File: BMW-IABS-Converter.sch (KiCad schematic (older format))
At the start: 43 parts, among them J1 SWD, J2 BMW_MOTORRAD, Q1 IRLML0060TRPbF, Q2 IRLML0060TRPbF, Q4 IRFR9024, Q6 IRFR9024, U1 SN65HVD230, U2 STM32F042F4P6, U3 MC34063AD, U4 LM2904

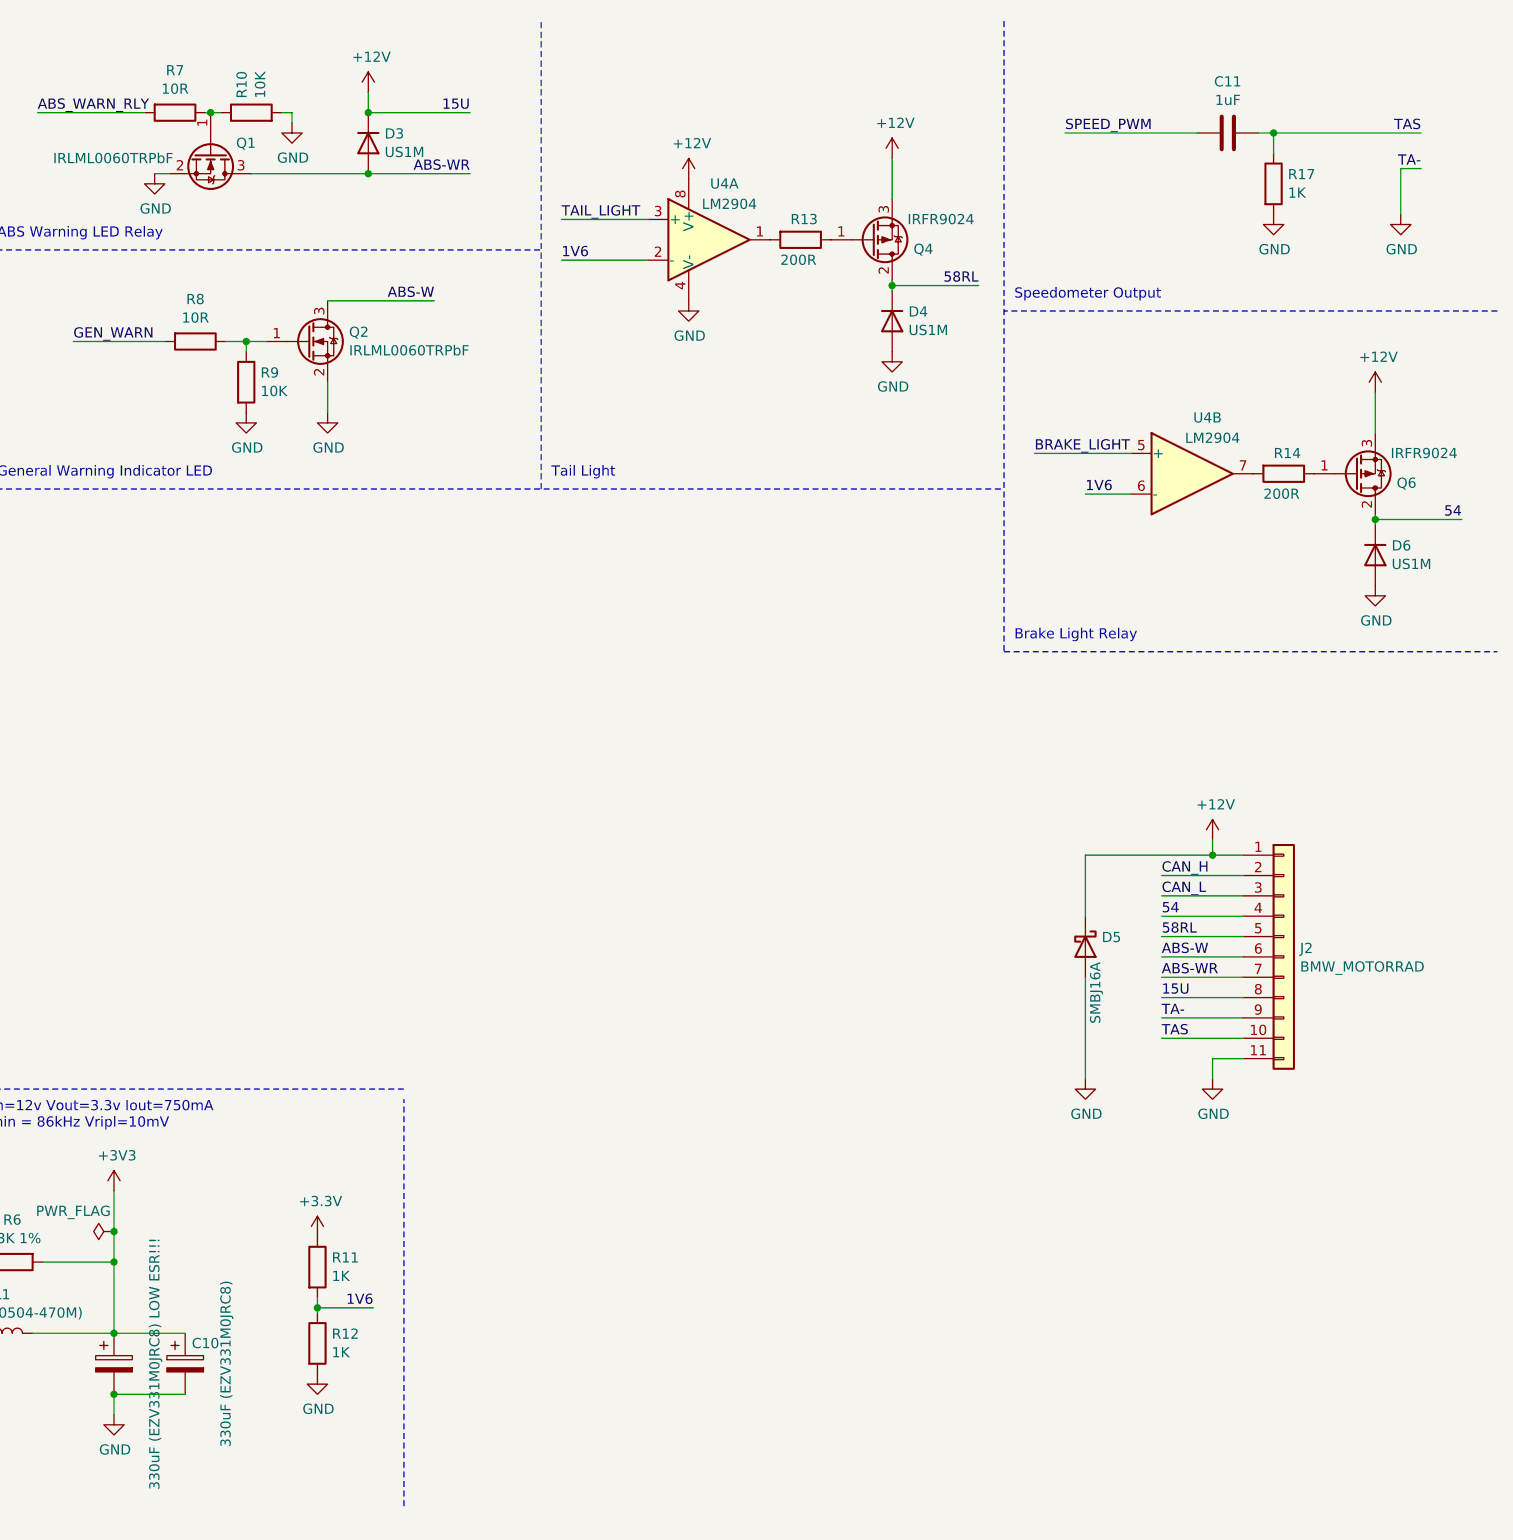
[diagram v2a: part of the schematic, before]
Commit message: Added connector footprint and symbol
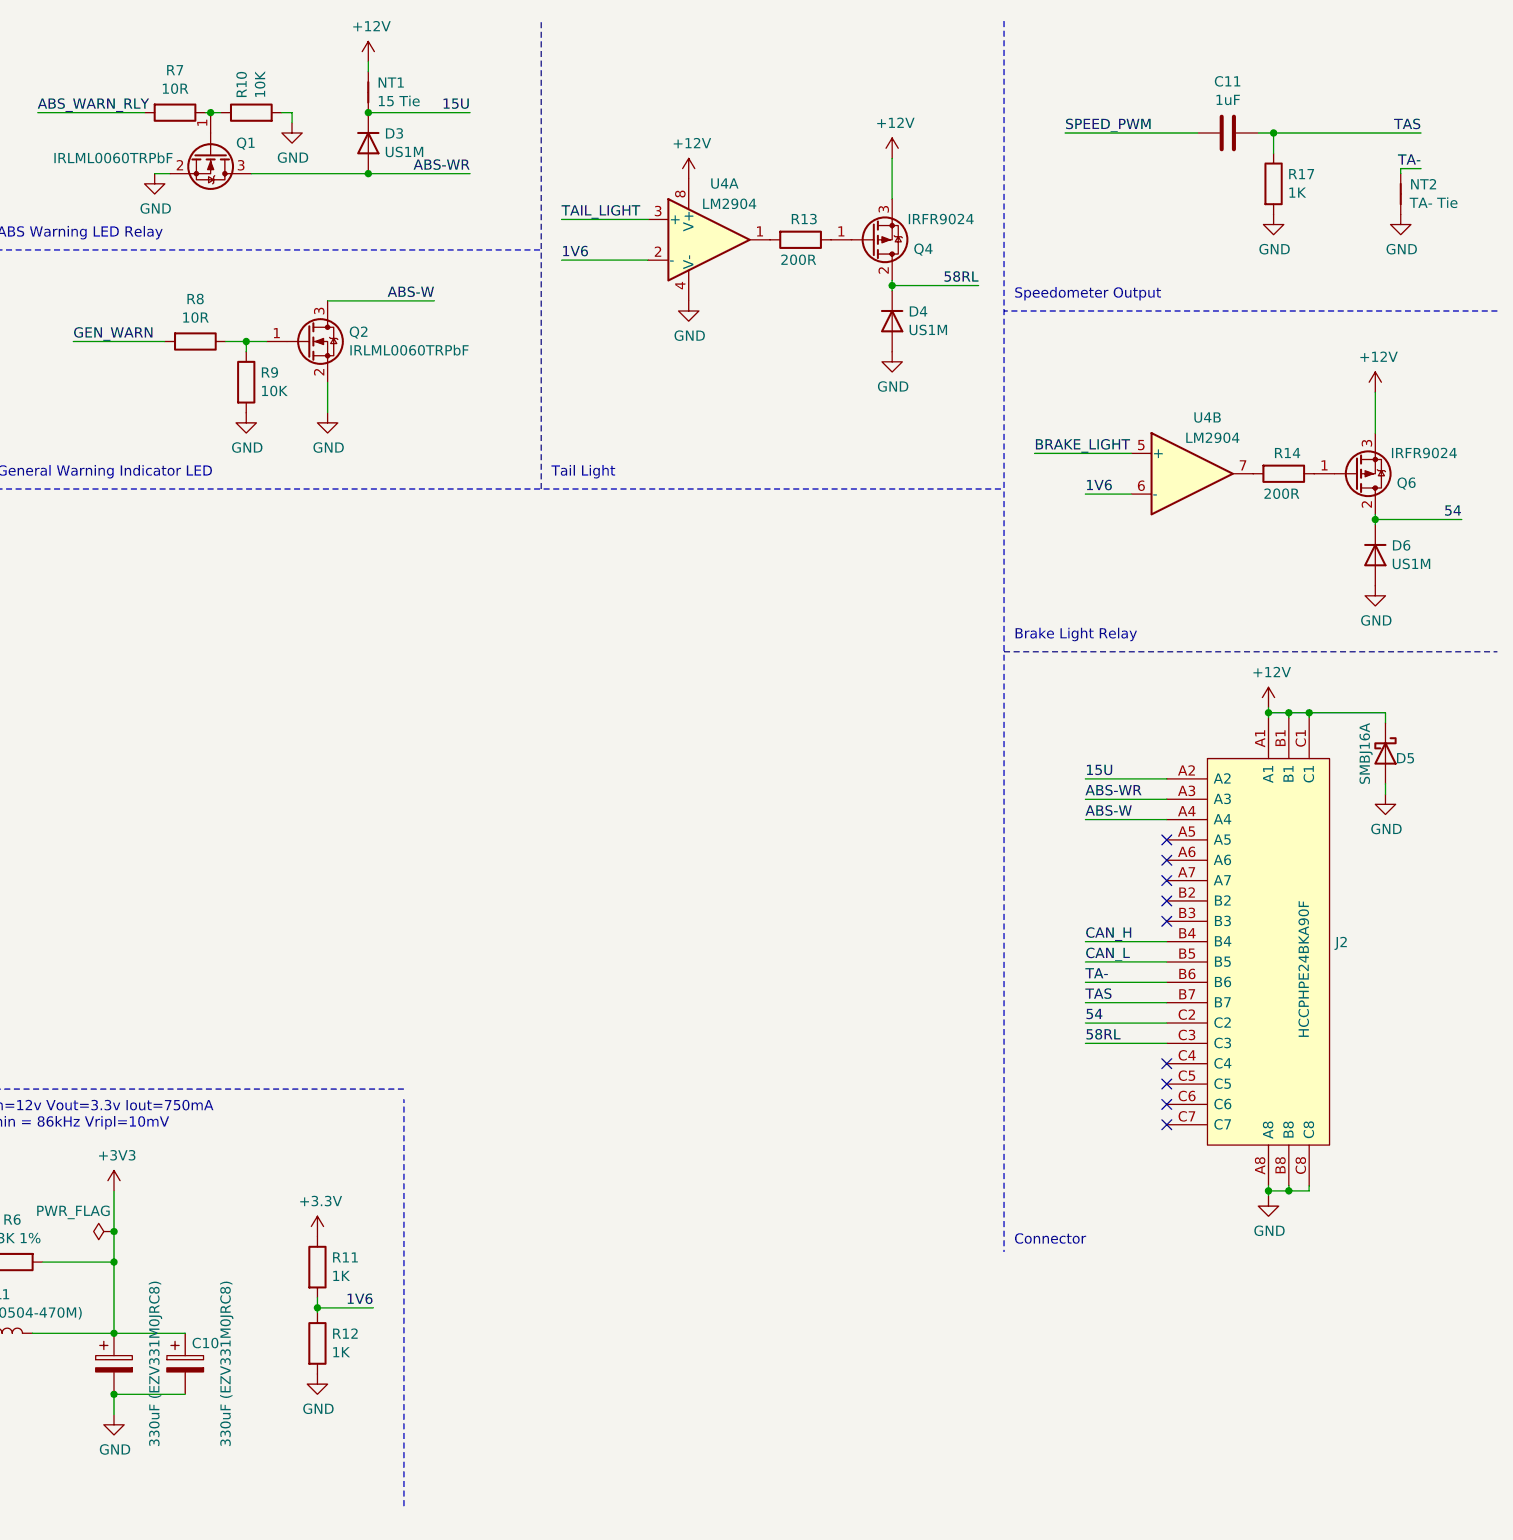
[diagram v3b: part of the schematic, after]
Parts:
- removed J2: BMW_MOTORRAD, symbol Connector_Generic:Conn_01x11
- added J2: HCCPHPE24BKA90F, HCCPHPE24BKA90F:HCCPHPE24BKA90F, symbol HCCPHPE24BKA90F:HCCPHPE24BKA90F
- added NT1: 15 Tie, NetTie:NetTie-2_SMD_Pad0.5mm, symbol Device:Net-Tie_2
- added NT2: TA- Tie, NetTie:NetTie-2_SMD_Pad0.5mm, symbol Device:Net-Tie_2
- C9: value 330uF (EZV331M0JRC8) LOW ESR!!! -> 330uF (EZV331M0JRC8); footprint (none) -> Capacitor_SMD:CP_Elec_6.3x7.7
- R11, R12: footprint (none) -> Resistor_SMD:R_0603_1608Metric
- U4: footprint (none) -> Package_SO:SOIC-8_3.9x4.9mm_P1.27mm
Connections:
- net +12V: now also J2.A1, J2.B1, J2.C1, NT1.1; no longer D3.1 (K)
- net 54: now also J2.C2
- net 58RL: now also J2.C3
- net ABS-W: now also J2.A4
- net ABS-WR: now also J2.A3
- net CAN_H: now also J2.B4
- net CAN_L: now also J2.B5
- net GND: now also J2.A8, J2.B8, J2.C8, NT2.2
- net TAS: now also J2.B7
- new net 15U: D3.1 (K), J2.A2, NT1.2
- new net TA-: J2.B6, NT2.1
- no-connect marks 7 -> 16
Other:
- note added: "Connector"
- moved on the sheet: D5
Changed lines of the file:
@@
 Text Label 3650 2575 2    50   ~ 0
 SWDIO
-$Comp
-L power:GND #PWR?
-U 1 1 60302FAE
-P 9825 5675
-AR Path="/602C3F48/60302FAE" Ref="#PWR?"  Part="1"
-AR Path="/60302FAE" Ref="#PWR035"  Part="1"
-F 0 "#PWR035" H 9825 5425 50  0001 C CNN
-F 1 "GND" H 9830 5502 50  0000 C CNN
-F 2 "" H 9825 5675 50  0001 C CNN
-F 3 "" H 9825 5675 50  0001 C CNN
-	1    9825 5675
-	1    0    0    -1
-$EndComp
-Wire Wire Line
-	9975 5575 9825 5575
-Wire Wire Line
-	9825 5575 9825 5675
-Wire Wire Line
-	9975 4675 9575 4675
-Text Label 9575 4675 0    50   ~ 0
+Wire Wire Line
+	9600 5000 9200 5000
+Text Label 9200 5000 0    50   ~ 0
 CAN_H
-Text Label 9575 4775 0    50   ~ 0
+Text Label 9200 5100 0    50   ~ 0
 CAN_L
 Wire Wire Line
-	9975 4775 9575 4775
-Wire Wire Line
-	9975 4575 9825 4575
-Wire Wire Line
-	9825 4575 9825 4500
+	9600 5100 9200 5100
 Wire Wire Line
 	2375 850  2375 1375
@@
 P 4425 7075
 F 0 "C9" H 4425 7075 50  0001 C CNN
-F 1 "330uF (EZV331M0JRC8) LOW ESR!!!" V 4625 7075 50  0000 C CNN
-F 2 "" H 4425 7075 50  0001 C CNN
+F 1 "330uF (EZV331M0JRC8)" V 4625 7075 50  0000 C CNN
+F 2 "Capacitor_SMD:CP_Elec_6.3x7.7" H 4425 7075 50  0001 C CNN
 F 3 "~" H 4425 7075 50  0001 C CNN
 F 4 "https://www.rcscomponents.kiev.ua/product/330uf-6-3v-ezv-smd-sizec8-6-3x7-7-low-imp-ezv331m0jrc8-elektroliticheskij-kondensator-smd-nizkoimpedansnyj_30350.html" H 4425 7075 50  0001 C CNN "Url"
@@
 L Device:D_Schottky D5
 U 1 1 6032D8FB
-P 9200 5025
-F 0 "D5" V 9154 5105 50  0000 L CNN
-F 1 "SMBJ16A" H 9275 5075 50  0000 L CNN
-F 2 "Diode_SMD:D_SMB" H 9200 5025 50  0001 C CNN
-F 3 "~" H 9200 5025 50  0001 C CNN
-	1    9200 5025
-	0    1    1    0
-$EndComp
-Wire Wire Line
-	9200 5175 9200 5675
+P 10675 4075
+F 0 "D5" V 10700 4125 50  0000 L CNN
+F 1 "SMBJ16A" H 10525 3975 50  0000 L CNN
+F 2 "Diode_SMD:D_SMB" H 10675 4075 50  0001 C CNN
+F 3 "~" H 10675 4075 50  0001 C CNN
+	1    10675 4075
+	0    1    1    0
+$EndComp
+Wire Wire Line
+	10675 4225 10675 4275
 $Comp
 L power:GND #PWR032
 U 1 1 6032D902
-P 9200 5675
-F 0 "#PWR032" H 9200 5425 50  0001 C CNN
-F 1 "GND" H 9205 5502 50  0000 C CNN
-F 2 "" H 9200 5675 50  0001 C CNN
-F 3 "" H 9200 5675 50  0001 C CNN
-	1    9200 5675
-	1    0    0    -1
-$EndComp
-Wire Wire Line
-	9200 4875 9200 4575
+P 10675 4275
+F 0 "#PWR032" H 10675 4025 50  0001 C CNN
+F 1 "GND" H 10680 4102 50  0000 C CNN
+F 2 "" H 10675 4275 50  0001 C CNN
+F 3 "" H 10675 4275 50  0001 C CNN
+	1    10675 4275
+	1    0    0    -1
+$EndComp
+Wire Wire Line
+	10675 3925 10675 3875
 $Comp
 L Device:CP C10
@@
 L power:+12V #PWR034
 U 1 1 6035EFEC
-P 9825 4500
-F 0 "#PWR034" H 9825 4350 50  0001 C CNN
-F 1 "+12V" H 9840 4673 50  0000 C CNN
-F 2 "" H 9825 4500 50  0001 C CNN
-F 3 "" H 9825 4500 50  0001 C CNN
-	1    9825 4500
+P 10100 3850
+F 0 "#PWR034" H 10100 3700 50  0001 C CNN
+F 1 "+12V" H 10115 4023 50  0000 C CNN
+F 2 "" H 10100 3850 50  0001 C CNN
+F 3 "" H 10100 3850 50  0001 C CNN
+	1    10100 3850
 	1    0    0    -1
 $EndComp
@@
 L power:+12V #PWR026
 U 1 1 6038C15A
-P 5675 825
-F 0 "#PWR026" H 5675 675 50  0001 C CNN
-F 1 "+12V" H 5690 998 50  0000 C CNN
-F 2 "" H 5675 825 50  0001 C CNN
-F 3 "" H 5675 825 50  0001 C CNN
-	1    5675 825
-	1    0    0    -1
-$EndComp
-Wire Wire Line
-	5675 825  5675 925
-Wire Wire Line
-	5675 925  6175 925
+P 5675 675
+F 0 "#PWR026" H 5675 525 50  0001 C CNN
+F 1 "+12V" H 5690 848 50  0000 C CNN
+F 2 "" H 5675 675 50  0001 C CNN
+F 3 "" H 5675 675 50  0001 C CNN
+	1    5675 675
+	1    0    0    -1
+$EndComp
+Wire Wire Line
+	5675 675  5675 725
 $Comp
 L Diode:US1M D3
@@
 	0    1    1    0
 $EndComp
-Connection ~ 5675 925
 Connection ~ 5675 1225
 Wire Wire Line
@@
 Wire Notes Line
 	8800 3575 11225 3575
-Wire Notes Line
-	8800 475  8800 3575
 Text Notes 6575 2725 0    50   ~ 0
 Tail Light
@@
 Wire Notes Line
 	3800 2775 8800 2775
-Text Label 9575 4875 0    50   ~ 0
+Text Label 9200 5400 0    50   ~ 0
 54
-Text Label 9575 5475 0    50   ~ 0
+Text Label 9200 5300 0    50   ~ 0
 TAS
-Text Label 9575 5375 0    50   ~ 0
+Text Label 9200 5200 0    50   ~ 0
 TA-
-Text Label 9575 4975 0    50   ~ 0
+Text Label 9200 5500 0    50   ~ 0
 58RL
-Text Label 9575 5175 0    50   ~ 0
+Text Label 9200 4300 0    50   ~ 0
 ABS-WR
-Text Label 9575 5275 0    50   ~ 0
+Text Label 9200 4200 0    50   ~ 0
 15U
-Text Label 9575 5075 0    50   ~ 0
+Text Label 9200 4400 0    50   ~ 0
 ABS-W
 Wire Wire Line
-	9575 5475 9975 5475
-Wire Wire Line
-	9575 5375 9975 5375
-Wire Wire Line
-	9575 5275 9975 5275
-Wire Wire Line
-	9575 5175 9975 5175
-Wire Wire Line
-	9575 5075 9975 5075
-Wire Wire Line
-	9575 4975 9975 4975
-Wire Wire Line
-	9575 4875 9975 4875
-$Comp
-L Connector_Generic:Conn_01x11 J2
-U 1 1 6069B512
-P 10175 5075
-F 0 "J2" H 10255 5117 50  0000 L CNN
-F 1 "BMW_MOTORRAD" H 10255 5026 50  0000 L CNN
-F 2 "" H 10175 5075 50  0001 C CNN
-F 3 "~" H 10175 5075 50  0001 C CNN
-	1    10175 5075
-	1    0    0    -1
-$EndComp
+	9200 5300 9600 5300
+Wire Wire Line
+	9200 5200 9600 5200
+Wire Wire Line
+	9200 4200 9600 4200
+Wire Wire Line
+	9200 4300 9600 4300
+Wire Wire Line
+	9200 4400 9600 4400
+Wire Wire Line
+	9200 5500 9600 5500
+Wire Wire Line
+	9200 5400 9600 5400
 Wire Wire Line
 	1325 6525 2175 6525
-Wire Wire Line
-	9200 4575 9825 4575
-Connection ~ 9825 4575
 Text Label 3650 1975 2    50   ~ 0
 TAIL_LIGHT
@@
 $EndComp
 Wire Wire Line
-	10750 1200 10750 1425
-Wire Wire Line
 	3650 1775 3075 1775
 Wire Wire Line
@@
 F 0 "U4" H 9800 2975 50  0000 C CNN
 F 1 "LM2904" H 9825 2875 50  0000 C CNN
-F 2 "" H 9725 2700 50  0001 C CNN
+F 2 "Package_SO:SOIC-8_3.9x4.9mm_P1.27mm" H 9725 2700 50  0001 C CNN
 F 3 "http://www.ti.com/lit/ds/symlink/lm358.pdf" H 9725 2700 50  0001 C CNN
 	2    9725 2700
@@
 F 0 "U4" H 7425 1825 50  0000 C CNN
 F 1 "LM2904" H 7450 1725 50  0000 C CNN
-F 2 "" H 7350 1550 50  0001 C CNN
+F 2 "Package_SO:SOIC-8_3.9x4.9mm_P1.27mm" H 7350 1550 50  0001 C CNN
 F 3 "http://www.ti.com/lit/ds/symlink/lm358.pdf" H 7350 1550 50  0001 C CNN
 	1    7350 1550
@@
 F 0 "U4" H 7308 1596 50  0001 L CNN
 F 1 "LM2904" H 7308 1505 50  0001 L CNN
-F 2 "" H 7350 1550 50  0001 C CNN
+F 2 "Package_SO:SOIC-8_3.9x4.9mm_P1.27mm" H 7350 1550 50  0001 C CNN
 F 3 "http://www.ti.com/lit/ds/symlink/lm358.pdf" H 7350 1550 50  0001 C CNN
 	3    7350 1550
@@
 F 0 "R11" H 5495 6646 50  0000 L CNN
 F 1 "1K" H 5495 6555 50  0000 L CNN
-F 2 "" V 5355 6600 50  0001 C CNN
+F 2 "Resistor_SMD:R_0603_1608Metric" V 5355 6600 50  0001 C CNN
 F 3 "~" H 5425 6600 50  0001 C CNN
 	1    5425 6600
@@
 F 0 "R12" H 5495 7021 50  0000 L CNN
 F 1 "1K" H 5495 6930 50  0000 L CNN
-F 2 "" V 5355 6975 50  0001 C CNN
+F 2 "Resistor_SMD:R_0603_1608Metric" V 5355 6975 50  0001 C CNN
 F 3 "~" H 5425 6975 50  0001 C CNN
 	1    5425 6975
@@
 Text Label 3650 2075 2    50   ~ 0
 GEN_WARN
+$Comp
+L HCCPHPE24BKA90F:HCCPHPE24BKA90F J2
+U 1 1 603C7357
+P 10100 5100
+F 0 "J2" H 10428 5196 50  0000 L CNN
+F 1 "HCCPHPE24BKA90F" V 10275 4725 50  0000 L CNN
+F 2 "HCCPHPE24BKA90F:HCCPHPE24BKA90F" V 10500 4750 50  0001 L CNN
+F 3 "https://componentsearchengine.com/Datasheets/1/HCCPHPE24BKA90F.pdf" H 10300 6000 50  0001 L CNN
+F 4 "Automotive Connectors 24 WAY PIN HEADER" V 10600 4300 50  0001 L CNN "Description"
+F 5 "Delphi" V 10500 4500 50  0001 L CNN "Manufacturer_Name"
+F 6 "HCCPHPE24BKA90F" V 10700 4750 50  0001 L CNN "Manufacturer_Part_Number"
+	1    10100 5100
+	1    0    0    -1
+$EndComp
+Wire Wire Line
+	10675 3875 10300 3875
+Wire Wire Line
+	10100 3850 10100 3875
+Wire Wire Line
+	10100 3875 10200 3875
+Wire Wire Line
+	10300 3875 10300 3900
+Connection ~ 10100 3875
+Wire Wire Line
+	10100 3875 10100 3900
+Wire Wire Line
+	10200 3875 10200 3900
+Connection ~ 10200 3875
+Wire Wire Line
+	10200 3875 10300 3875
+Connection ~ 10300 3875
+$Comp
+L power:GND #PWR0105
+U 1 1 60420CEE
+P 10100 6250
+F 0 "#PWR0105" H 10100 6000 50  0001 C CNN
+F 1 "GND" H 10105 6077 50  0000 C CNN
+F 2 "" H 10100 6250 50  0001 C CNN
+F 3 "" H 10100 6250 50  0001 C CNN
+	1    10100 6250
+	1    0    0    -1
+$EndComp
+Wire Wire Line
+	10100 6200 10100 6225
+Wire Wire Line
+	10100 6225 10200 6225
+Wire Wire Line
+	10300 6225 10300 6200
+Connection ~ 10100 6225
+Wire Wire Line
+	10100 6225 10100 6250
+Wire Wire Line
+	10200 6200 10200 6225
+Connection ~ 10200 6225
+Wire Wire Line
+	10200 6225 10300 6225
+NoConn ~ 9600 4500
+NoConn ~ 9600 4600
+NoConn ~ 9600 4700
+NoConn ~ 9600 4800
+NoConn ~ 9600 4900
+NoConn ~ 9600 5600
+NoConn ~ 9600 5700
+NoConn ~ 9600 5800
+NoConn ~ 9600 5900
+Wire Notes Line
+	8800 475  8800 6525
+Text Notes 8850 6500 0    50   ~ 0
+Connector
+$Comp
+L Device:Net-Tie_2 NT2
+U 1 1 6051797D
+P 10750 1325
+F 0 "NT2" V 10704 1369 50  0000 L CNN
+F 1 "TA- Tie" V 10795 1369 50  0000 L CNN
+F 2 "NetTie:NetTie-2_SMD_Pad0.5mm" H 10750 1325 50  0001 C CNN
+F 3 "~" H 10750 1325 50  0001 C CNN
+	1    10750 1325
+	0    1    1    0
+$EndComp
+Wire Wire Line
+	10750 1200 10750 1225
+$Comp
+L Device:Net-Tie_2 NT1
+U 1 1 60524AB4
+P 5675 825
+F 0 "NT1" V 5629 869 50  0000 L CNN
+F 1 "15 Tie" V 5720 869 50  0000 L CNN
+F 2 "NetTie:NetTie-2_SMD_Pad0.5mm" H 5675 825 50  0001 C CNN
+F 3 "~" H 5675 825 50  0001 C CNN
+	1    5675 825
+	0    1    1    0
+$EndComp
+Connection ~ 5675 925
+Wire Wire Line
+	5675 925  6175 925
 $EndSCHEMATC

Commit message: Updated schematic and layout
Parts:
- removed NT1: 15 Tie, NetTie:NetTie-2_SMD_Pad0.5mm, symbol Device:Net-Tie_2
- added D7: US1M, Diode_SMD:D_SMA, symbol Diode:US1M
- added H1, H2, H3, H4: MountingHole, MountingHole:MountingHole_3.2mm_M3, symbol Mechanical:MountingHole
- added J3: GPIO_A0, Connector_PinHeader_1.27mm:PinHeader_1x01_P1.27mm_Vertical, symbol Connector_Generic:Conn_01x01
- added J4: GPIO_A1, Connector_PinHeader_1.27mm:PinHeader_1x01_P1.27mm_Vertical, symbol Connector_Generic:Conn_01x01
- added J5: GPIO_F0, Connector_PinHeader_1.27mm:PinHeader_1x01_P1.27mm_Vertical, symbol Connector_Generic:Conn_01x01
- added J6: GPIO_F1, Connector_PinHeader_1.27mm:PinHeader_1x01_P1.27mm_Vertical, symbol Connector_Generic:Conn_01x01
- added J7: GPIO_A2, Connector_PinHeader_1.27mm:PinHeader_1x01_P1.27mm_Vertical, symbol Connector_Generic:Conn_01x01
- added J8: GND, Connector_PinHeader_1.27mm:PinHeader_1x01_P1.27mm_Vertical, symbol Connector_Generic:Conn_01x01
- added LOGO1: Logo_Open_Hardware_Small, Symbol:OSHW-Symbol_6.7x6mm_SilkScreen, symbol Graphic:Logo_Open_Hardware_Small
- added LOGO2: Sine_Logo_S, sine:sine_logo_small, symbol sine:Sine_Logo_S
- C11: footprint Capacitor_SMD:C_0603_1608Metric -> Capacitor_SMD:C_0805_2012Metric
- C6: footprint Capacitor_SMD:C_0603_1608Metric -> Capacitor_SMD:C_0402_1005Metric
- L1: value 47uH (SND0504-470M) -> 18uH (SND0504-180M)
- Q1, Q2: value IRLML0060TRPbF -> IRLML0030TRPbF
- R13, R14: footprint Capacitor_SMD:C_0402_1005Metric -> Resistor_SMD:R_0603_1608Metric
- R17: footprint Capacitor_SMD:C_0402_1005Metric -> Resistor_SMD:R_0402_1005Metric
- R7, R8: value 10R -> 100R
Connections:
- net labels added: GPIO_A0, GPIO_A1, GPIO_A2, GPIO_F0, GPIO_F1
- wire segments 145 -> 154
- no-connect marks 16 -> 13
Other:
- note added: "GPIO"
- moved on the sheet: D4, D5, J2, Q2, Q4, R13, R2, R8, R9, U4A, U4B
